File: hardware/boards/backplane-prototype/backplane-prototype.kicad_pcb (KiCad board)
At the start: 4 copper layers, 151.8 x 30.8 mm, 93 parts, among them J1 SLOT_1, J10 SWD, J11 12V 3-WIRE FAN, J12 DS18B20 EXT SUPPLY, J2 XY308-2.54-3P / EXTERNAL CAN, J3 SLOT_2, J4 SLOT_3, J5 DC IN, J6 SLOT_4, J7 SLOT_5, J8 SLOT_6, J9 12V 3-WIRE FAN, Q1 AO3407A, Q2 2N7002, Q3 AO3407A, Q4 2N7002, U1 STM32C092GCU6, U2 LM5164DDAR, U3 LM5164DDAR, U4 INA237AIDGSR, U5 TCAN3413DR

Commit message: checkpoint: save revised INA237 layout
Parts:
- moved C16 12.5 mm to (44.2, 73.1), turned to 90 degrees
- moved U4 9.34 mm to (48.6, 73.4)
- moved R12 9.26 mm to (50.8, 70.7)
- moved C15 9.24 mm to (47.7, 70.7)
- moved R11 9.24 mm to (44.7, 70.7)
- moved R15 5.23 mm to (41.6, 71.5), turned to 180 degrees
- moved R14 4.00 mm to (41.6, 74.8), turned to 180 degrees
- moved R13 3.28 mm to (41.6, 73.1), turned to 180 degrees
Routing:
- net I2C_SCL: track 145.4 -> 159.3 mm
- net I2C_SDA: track 147.2 -> 160.6 mm
- net VCC: track 7.00 -> 17.4 mm
- net INA_ALERT: track 146.6 -> 156.6 mm, vias 2 -> 3
- net +3V3: track 265.3 -> 274.8 mm, vias 6 -> 5
- net GND: track 32.7 -> 41.0 mm, vias 54 -> 61
- net /Power Input and Monitor/INA_IN_N: track 0.00 -> 4.92 mm
- net VIN_RAW: track 0.00 -> 4.07 mm
- net /Power Input and Monitor/INA_IN_P: track 0.00 -> 3.32 mm

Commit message: checkpoint: save INA layout refinements
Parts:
- moved TP7 18.6 mm to (49.6, 40.0)
- moved TP16 15.3 mm to (33.7, 38.9)
- moved H1 11.4 mm to (40.2, 38.0)
- moved TP6 11.4 mm to (52.6, 39.2)
- moved TP15 10.2 mm to (46.6, 38.6)
- moved D1 4.03 mm to (39.4, 50.3)
- moved L3 4.01 mm to (44.4, 50.2)
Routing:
- net /CAN-FD and Six Slots/CAN_EXT_P: track 11.2 -> 0.13 mm
- net /CAN-FD and Six Slots/CAN_EXT_N: track 11.0 -> 0.00 mm
- net /CAN-FD and Six Slots/CAN_BUS_P: track 147.8 -> 140.1 mm
- net /CAN-FD and Six Slots/CAN_BUS_N: track 138.3 -> 132.2 mm
- net CAN_TX: track 106.0 -> 103.4 mm
- net CAN_RX: track 108.9 -> 106.3 mm
- net GND: vias 61 -> 58
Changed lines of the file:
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@@
 	(footprint "mini-rack-power:MountingHole_2.2mm_M2_Pad_Via_JLC"
 		(layer "F.Cu")
-		(at 39.3 49.4)
+		(at 40.175349 38.014701)
 		(descr "Mounting Hole 2.2mm, M2, with 0.3 mm stitching drills, 0.26 mm annular rings, and 0.45 mm hole clearance")
 		(tags "mountinghole M2 JLCPCB")
@@
 	(footprint "TestPoint:TestPoint_Pad_D1.5mm"
 		(layer "B.Cu")
-		(at 53.415463 50.521036 180)
+		(at 52.63496 39.184908 180)
 		(descr "SMD pad as test Point, diameter 1.5mm")
 		(tags "test point SMD pad")
@@
 	(footprint "TestPoint:TestPoint_Pad_D1.5mm"
 		(layer "B.Cu")
-		(at 53.423993 58.146603 180)
+		(at 49.566351 39.965287 180)
 		(descr "SMD pad as test Point, diameter 1.5mm")
 		(tags "test point SMD pad")
@@
 	(footprint "TestPoint:TestPoint_Pad_D1.5mm"
 		(layer "B.Cu")
-		(at 42.76 47.98 180)
+		(at 46.643236 38.56325 180)
 		(descr "SMD pad as test Point, diameter 1.5mm")
 		(tags "test point SMD pad")
@@
 	(footprint "mini-rack-power:L_CommonModeChoke_TDK_ACT1210D"
 		(layer "B.Cu")
-		(at 44.42 54.23 180)
+		(at 44.394686 50.216028 180)
 		(descr "TDK ACT1210D automotive CAN/CAN-FD common-mode choke, 3.2 x 2.5 mm body; manufacturer recommended 4.1 x 1.6 mm land pattern")
 		(tags "common mode choke CAN CAN-FD TDK ACT1210D C3039743")
@@
 	(footprint "TestPoint:TestPoint_Pad_D1.5mm"
 		(layer "B.Cu")
-		(at 42.76 51.19 180)
+		(at 33.720689 38.907146 180)
 		(descr "SMD pad as test Point, diameter 1.5mm")
 		(tags "test point SMD pad")
@@
 	(footprint "Package_TO_SOT_SMD:SOT-23"
 		(layer "B.Cu")
-		(at 39.28 54.28)
+		(at 39.447877 50.255709)
 		(descr "SOT, 3 Pin (JEDEC TO-236 Var AB https://www.jedec.org/document_search?search_api_views_fulltext=TO-236)")
 		(tags "SOT TO_SOT_SMD")
@@
 	)
 	(via
-		(at 41.693468 54.28)
-		(size 0.6)
-		(drill 0.3)
-		(layers "F.Cu" "B.Cu")
-		(free yes)
-		(net "GND")
-	)
-	(via
 		(at 63.86 72.18)
 		(size 0.6)
@@
 	)
 	(via
-		(at 35.990685 48.835)
-		(size 0.6)
-		(drill 0.3)
-		(layers "F.Cu" "B.Cu")
-		(free yes)
-		(net "GND")
-	)
-	(via
 		(at 63.2575 70.44)
 		(size 0.6)
@@
 	)
 	(via
-		(at 35.990685 52.356048)
-		(size 0.6)
-		(drill 0.3)
-		(layers "F.Cu" "B.Cu")
-		(free yes)
-		(net "GND")
-	)
-	(via
 		(at 30.861668 48.835)
 		(size 0.6)
@@
 	)
 	(segment
-		(start 45.07 48.65)
-		(end 44.88 48.65)
-		(width 0.2)
-		(layer "B.Cu")
-		(net "/CAN-FD and Six Slots/CAN_BUS_P")
-	)
-	(segment
 		(start 164.795 55.30132)
 		(end 165.145 54.95132)
@@
 	)
 	(segment
-		(start 44.88 48.65)
-		(end 44.21 47.98)
-		(width 0.2)
-		(layer "B.Cu")
-		(net "/CAN-FD and Six Slots/CAN_BUS_P")
-	)
-	(segment
 		(start 69.795 57.420624)
 		(end 69.795 57.155)
@@
 	)
 	(segment
-		(start 44.21 47.98)
-		(end 42.76 47.98)
-		(width 0.2)
-		(layer "B.Cu")
-		(net "/CAN-FD and Six Slots/CAN_BUS_P")
-	)
-	(segment
-		(start 45.755 53.54)
-		(end 45.755 50.285)
-		(width 0.2)
-		(layer "B.Cu")
-		(net "/CAN-FD and Six Slots/CAN_BUS_P")
-	)
-	(segment
 		(start 69.795 57.155)
 		(end 71.8 55.15)
@@
 	)
 	(segment
-		(start 45.07 49.6)
-		(end 45.07 48.65)
-		(width 0.2)
-		(layer "B.Cu")
-		(net "/CAN-FD and Six Slots/CAN_BUS_P")
-	)
-	(segment
 		(start 126.795 55.15)
 		(end 126.795 57.420624)
@@
 	)
 	(segment
-		(start 45.755 50.285)
-		(end 45.07 49.6)
-		(width 0.2)
-		(layer "B.Cu")
-		(net "/CAN-FD and Six Slots/CAN_BUS_P")
-	)
-	(segment
 		(start 59.942698 55.408837)
 		(end 67.783213 55.408837)
@@
 	)
 	(segment
-		(start 44.805 50.97)
-		(end 42.89 50.97)
-		(width 0.2)
-		(layer "B.Cu")
-		(net "/CAN-FD and Six Slots/CAN_BUS_N")
-	)
-	(segment
 		(start 48.05 54.96)
 		(end 48.02 54.93)
@@
 	)
 	(segment
-		(start 44.805 50.97)
-		(end 44.805 54.315)
-		(width 0.2)
-		(layer "B.Cu")
-		(net "/CAN-FD and Six Slots/CAN_BUS_N")
-	)
-	(segment
 		(start 47.82 54.73)
 		(end 48.02 54.93)
@@
 	)
 	(segment
-		(start 44.805 54.315)
-		(end 45.22 54.73)
-		(width 0.2)
-		(layer "B.Cu")
-		(net "/CAN-FD and Six Slots/CAN_BUS_N")
-	)
-	(segment
-		(start 42.89 50.97)
-		(end 42.67 51.19)
-		(width 0.2)
-		(layer "B.Cu")
-		(net "/CAN-FD and Six Slots/CAN_BUS_N")
-	)
-	(segment
 		(start 45.22 54.73)
 		(end 45.945 54.73)
@@
 	)
 	(segment
-		(start 53.415463 50.521036)
-		(end 51.56534 52.371159)
-		(width 0.2)
-		(layer "B.Cu")
-		(net "CAN_TX")
-	)
-	(segment
 		(start 146.176193 50.728797)
 		(end 148.584413 48.320577)
@@
 	)
 	(segment
-		(start 53.423993 58.146603)
-		(end 51.589687 56.312297)
-		(width 0.2)
-		(layer "B.Cu")
-		(net "CAN_RX")
-	)
-	(segment
 		(start 145.99651 51.527071)
 		(end 148.67443 48.849151)
@@
 	)
 	(segment
-		(start 35.675 53.33)
-		(end 37.575 55.23)
-		(width 0.2)
-		(layer "B.Cu")
-		(net "/CAN-FD and Six Slots/CAN_EXT_N")
-	)
-	(segment
-		(start 42.395 55.23)
-		(end 42.895 54.73)
-		(width 0.2)
-		(layer "B.Cu")
-		(net "/CAN-FD and Six Slots/CAN_EXT_N")
-	)
-	(segment
-		(start 37.575 55.23)
-		(end 38.3425 55.23)
-		(width 0.2)
-		(layer "B.Cu")
-		(net "/CAN-FD and Six Slots/CAN_EXT_N")
-	)
-	(segment
-		(start 38.3425 55.23)
-		(end 42.395 55.23)
-		(width 0.2)
-		(layer "B.Cu")
-		(net "/CAN-FD and Six Slots/CAN_EXT_N")
-	)
-	(segment
-		(start 33.72 51.375)
-		(end 35.675 53.33)
-		(width 0.2)
-		(layer "B.Cu")
-		(net "/CAN-FD and Six Slots/CAN_EXT_N")
-	)
-	(segment
-		(start 42.495 53.33)
-		(end 42.895 53.73)
-		(width 0.2)
-		(layer "B.Cu")
-		(net "/CAN-FD and Six Slots/CAN_EXT_P")
-	)
-	(segment
-		(start 38.3425 53.33)
-		(end 33.8475 48.835)
-		(width 0.2)
-		(layer "B.Cu")
-		(net "/CAN-FD and Six Slots/CAN_EXT_P")
-	)
-	(segment
-		(start 38.3425 53.33)
-		(end 42.495 53.33)
-		(width 0.2)
-		(layer "B.Cu")
-		(net "/CAN-FD and Six Slots/CAN_EXT_P")
-	)
-	(segment

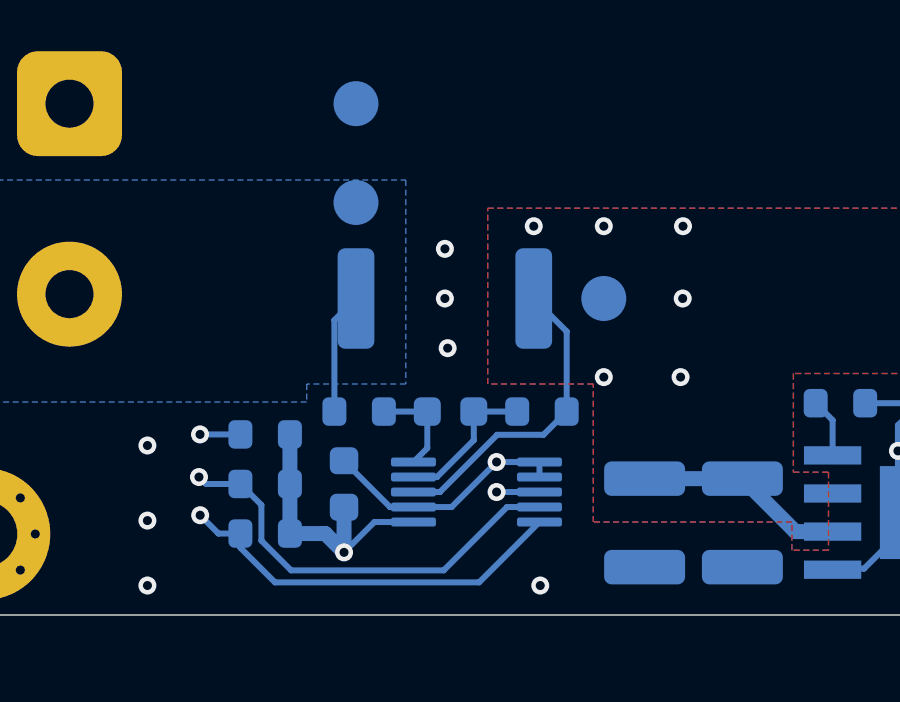
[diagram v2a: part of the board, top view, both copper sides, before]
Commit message: Refine INA237 Kelvin sense pickups
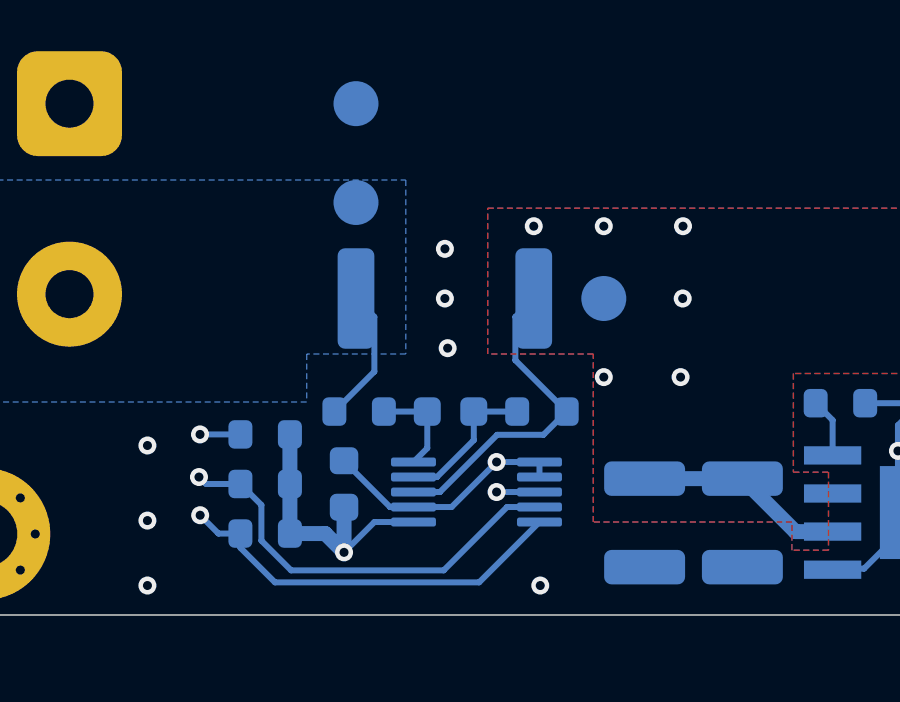
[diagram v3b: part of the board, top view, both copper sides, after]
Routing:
- net VCC: track 17.4 -> 17.9 mm
- net VIN_RAW: track 4.07 -> 4.57 mm
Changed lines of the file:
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@@
 	)
 	(segment
+		(start 49.9025 69.007922)
+		(end 49.9025 67.5625)
+		(width 0.2)
+		(layer "B.Cu")
+		(net "VCC")
+	)
+	(segment
 		(start 49.295279 71.493604)
 		(end 47.388241 73.400642)
@@
 	)
 	(segment
-		(start 51.613182 68.048182)
+		(start 49.9025 67.5625)
 		(end 50.515 66.95)
 		(width 0.2)
@@
 	(segment
 		(start 51.613182 70.718604)
-		(end 51.613182 68.048182)
+		(end 49.9025 69.007922)
 		(width 0.2)
 		(layer "B.Cu")
@@
 	)
 	(segment
+		(start 45.2025 69.38569)
+		(end 45.2025 67.5625)
+		(width 0.2)
+		(layer "B.Cu")
+		(net "VIN_RAW")
+	)
+	(segment
 		(start 43.869586 70.718604)
-		(end 43.869586 67.670414)
+		(end 45.2025 69.38569)
 		(width 0.2)
 		(layer "B.Cu")
@@
 	)
 	(segment
-		(start 43.869586 67.670414)
+		(start 45.2025 67.5625)
 		(end 44.59 66.95)
 		(width 0.2)
@@
 				(xy 48.98 63.94) (xy 168.25 63.94) (xy 168.25 72.5) (xy 123.75 72.5) (xy 123.75 69.45) (xy 59.17 69.45)
 				(xy 59.17 72.74) (xy 60.34 72.74) (xy 60.34 75.34) (xy 59.12 75.34) (xy 59.12 74.4) (xy 52.5 74.4)
-				(xy 52.5 69.8) (xy 48.98 69.8)
+				(xy 52.5 68.8) (xy 48.98 68.8)
 			)
 		)
@@
 		(polygon
 			(pts
-				(xy 31.998496 63) (xy 46.25 63) (xy 46.25 69.80008) (xy 42.94669 69.80008) (xy 42.94669 70.4) (xy 31.998496 70.4)
+				(xy 31.998496 63) (xy 46.25 63) (xy 46.25 68.8) (xy 42.94669 68.8) (xy 42.94669 70.4) (xy 31.998496 70.4)
 			)
 		)

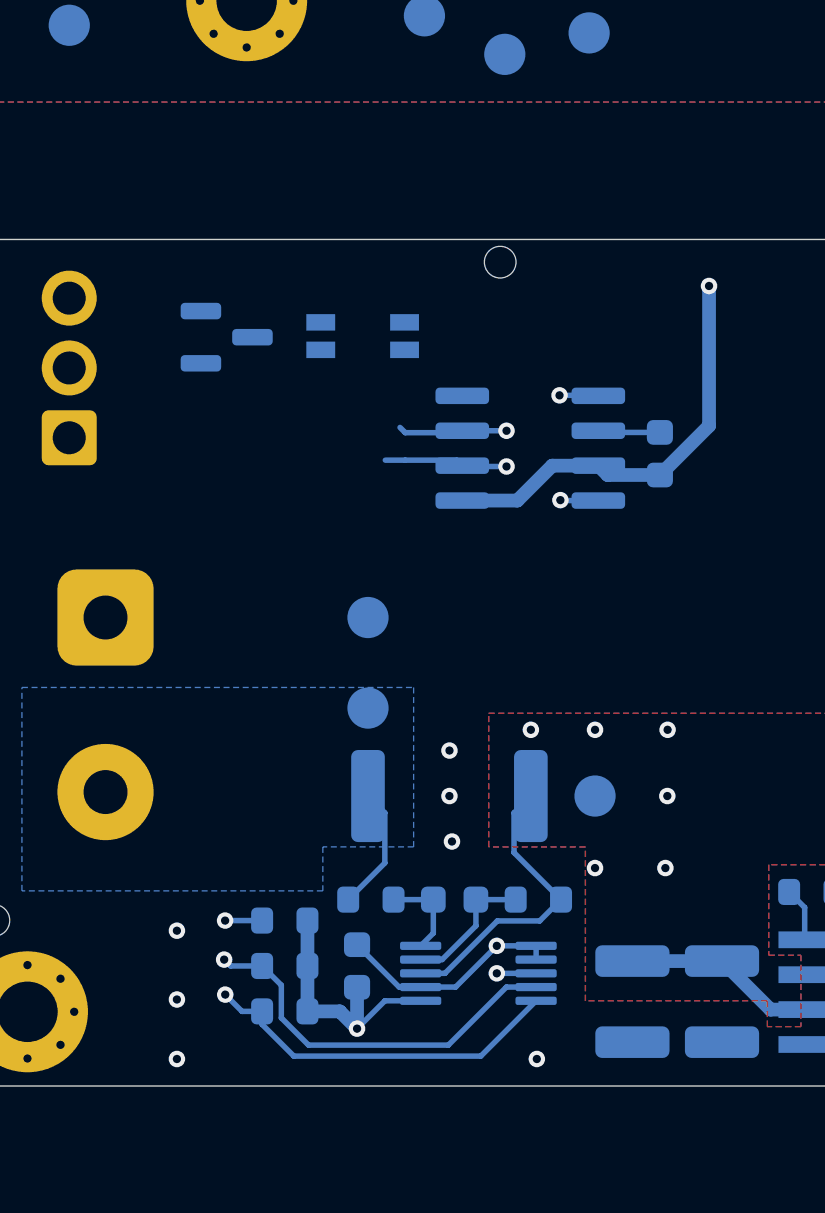
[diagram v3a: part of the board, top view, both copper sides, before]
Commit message: Center CAN protection diode at J2
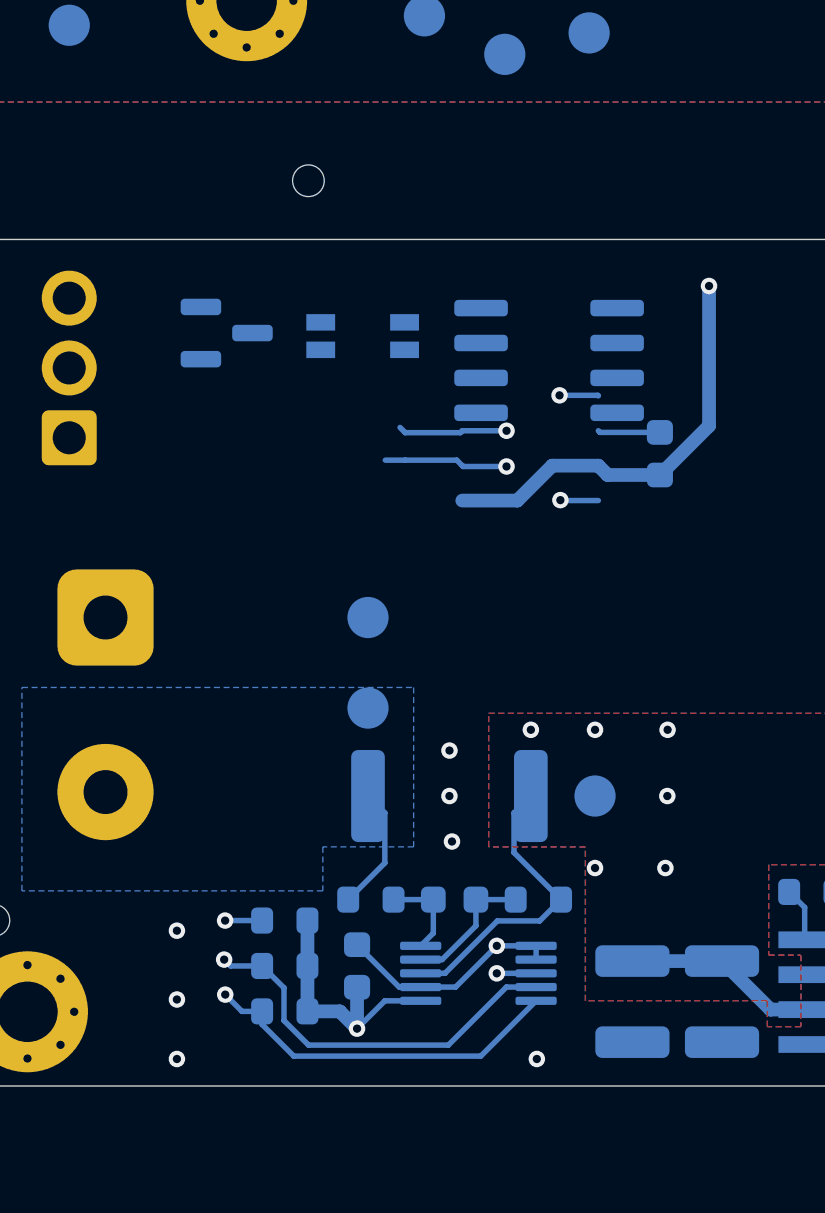
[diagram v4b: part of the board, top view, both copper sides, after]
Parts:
- moved H9 7.58 mm to (42.4, 44.6)
- moved U5 3.26 mm to (51.2, 51.1)
- moved D1 0.15 mm to (39.4, 50.1)
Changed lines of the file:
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@@
 	(footprint "mini-rack-power:MountingHole_JLCPCB_Tooling_1.152mm"
 		(layer "B.Cu")
-		(at 49.4 47.526 180)
+		(at 42.422036 44.563462 180)
 		(descr "JLCPCB PCBA tooling hole: 1.152 mm round NPTH with 0.148 mm solder-mask expansion")
 		(tags "mountinghole tooling JLCPCB PCBA NPTH 1.152mm")
@@
 	(footprint "Package_SO:SOIC-8_3.9x4.9mm_P1.27mm"
 		(layer "B.Cu")
-		(at 50.495 54.295 180)
+		(at 51.17833 51.102311 180)
 		(descr "SOIC, 8 Pin (JEDEC MS-012AA, https://www.analog.com/media/en/package-pcb-resources/package/pkg_pdf/soic_narrow-r/r_8.pdf)")
 		(tags "SOIC SO")
@@
 	(footprint "Package_TO_SOT_SMD:SOT-23"
 		(layer "B.Cu")
-		(at 39.447877 50.255709)
+		(at 39.447877 50.105)
 		(descr "SOT, 3 Pin (JEDEC TO-236 Var AB https://www.jedec.org/document_search?search_api_views_fulltext=TO-236)")
 		(tags "SOT TO_SOT_SMD")
@@
 	)
 	(segment
-		(start 41.437035 73.832896)
-		(end 40.737035 73.132896)
+		(start 50.705831 73.900642)
+		(end 49.624884 73.900642)
 		(width 0.2)
 		(layer "B.Cu")
@@
 	)
 	(segment
-		(start 47.513014 76.012512)
-		(end 42.426859 76.012512)
+		(start 149.010108 50.807752)
+		(end 149.396684 50.421176)
 		(width 0.2)
 		(layer "B.Cu")
@@
 	)
 	(segment
-		(start 41.437035 75.022688)
-		(end 41.437035 73.832896)
+		(start 145.005647 50.105008)
+		(end 145.60784 50.105008)
 		(width 0.2)
 		(layer "B.Cu")
@@
 	)
 	(segment
-		(start 149.010108 50.807752)
-		(end 149.396684 50.421176)
+		(start 42.426859 76.012512)
+		(end 41.533848 75.119501)
 		(width 0.2)
 		(layer "B.Cu")
@@
 	)
 	(segment
-		(start 50.705831 73.900642)
-		(end 49.624884 73.900642)
+		(start 142.960993 48.060354)
+		(end 145.005647 50.105008)
 		(width 0.2)
 		(layer "B.Cu")
@@
 	)
 	(segment
-		(start 145.005647 50.105008)
-		(end 145.60784 50.105008)
+		(start 40.737035 73.132896)
+		(end 39.594807 73.132896)
 		(width 0.2)
 		(layer "B.Cu")
@@
 	)
 	(segment
-		(start 49.624884 73.900642)
-		(end 47.513014 76.012512)
+		(start 41.533848 73.929709)
+		(end 40.737035 73.132896)
 		(width 0.2)
 		(layer "B.Cu")
@@
 	)
 	(segment
-		(start 142.960993 48.060354)
-		(end 145.005647 50.105008)
+		(start 41.533848 75.119501)
+		(end 41.533848 73.929709)
 		(width 0.2)
 		(layer "B.Cu")
@@
 	)
 	(segment
-		(start 40.737035 73.132896)
-		(end 39.594807 73.132896)
+		(start 39.594807 73.132896)
+		(end 39.356049 72.894138)
 		(width 0.2)
 		(layer "B.Cu")
@@
 	)
 	(segment
-		(start 42.426859 76.012512)
-		(end 41.437035 75.022688)
+		(start 49.624884 73.900642)
+		(end 47.513014 76.012512)
 		(width 0.2)
 		(layer "B.Cu")
@@
 	)
 	(segment
-		(start 39.594807 73.132896)
-		(end 39.356049 72.894138)
+		(start 47.513014 76.012512)
+		(end 42.426859 76.012512)
 		(width 0.2)
 		(layer "B.Cu")
